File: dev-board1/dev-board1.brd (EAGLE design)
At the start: 100 x 80 mm, 127 parts, among them IC1 MSP432E401, IC2 MT48LC16M16A2, IC3 SIM800C, IC4 CC3100MOD-LWK, IC5 TPD3E001DRL, IC6 TPD3E001DRL, IC7 TPD3E001DRL, IC8 BQ25601, IC9 TPS62082, J1 MAGJACK-RJMG16XXX-8, J2 SIM-78723-1001, J3 ER-TFT024-3, J4 SWD_SHROUD, Q6 CSD25402Q3A, U3 ER-TFT024-3-OUTLINE, X2 BU-SMA-V

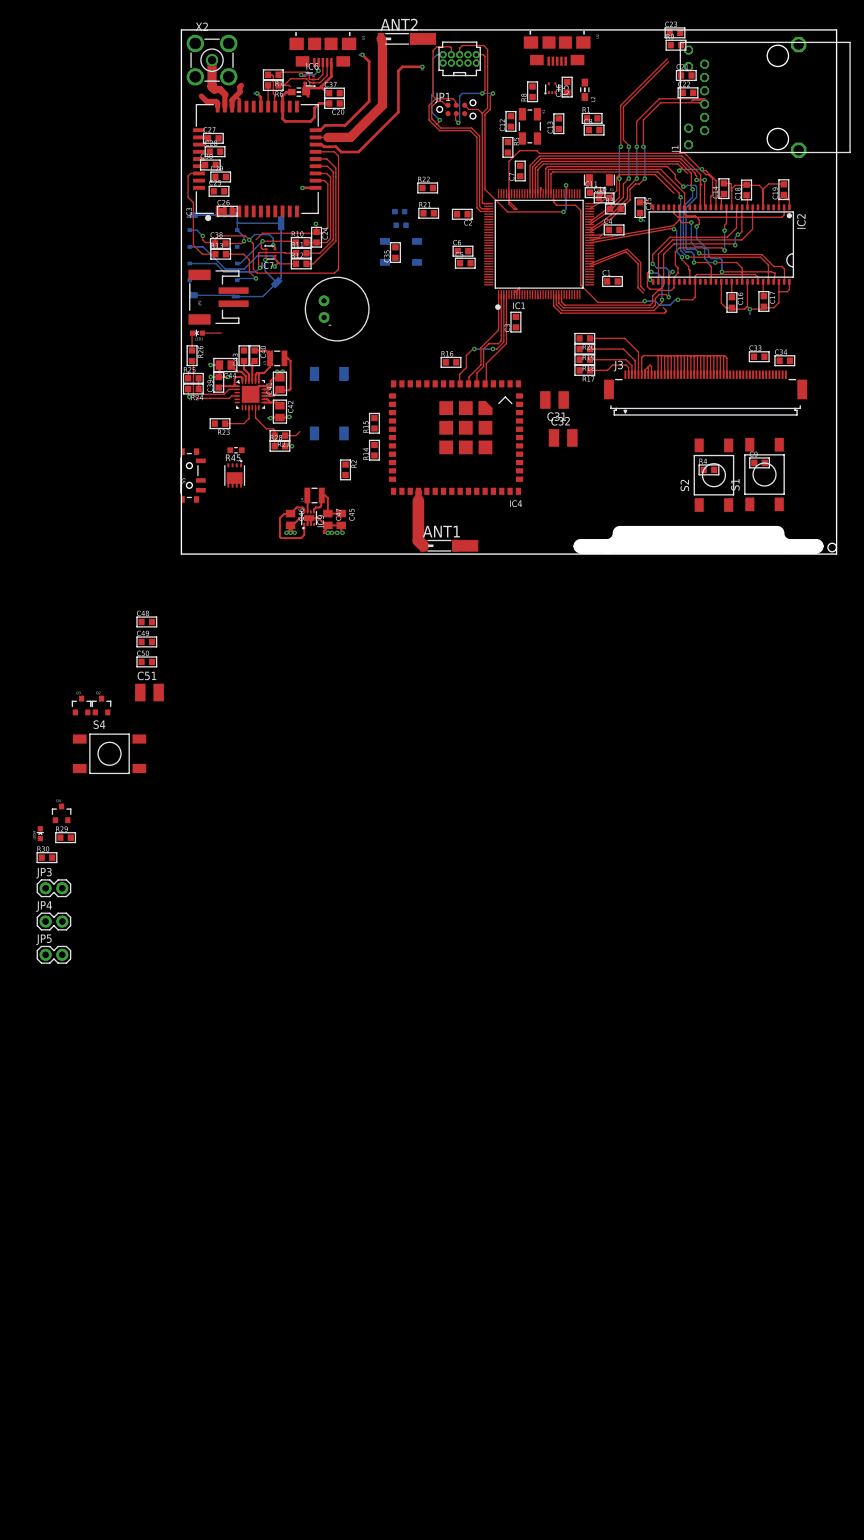
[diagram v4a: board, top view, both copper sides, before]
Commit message: changing to cc3120miod
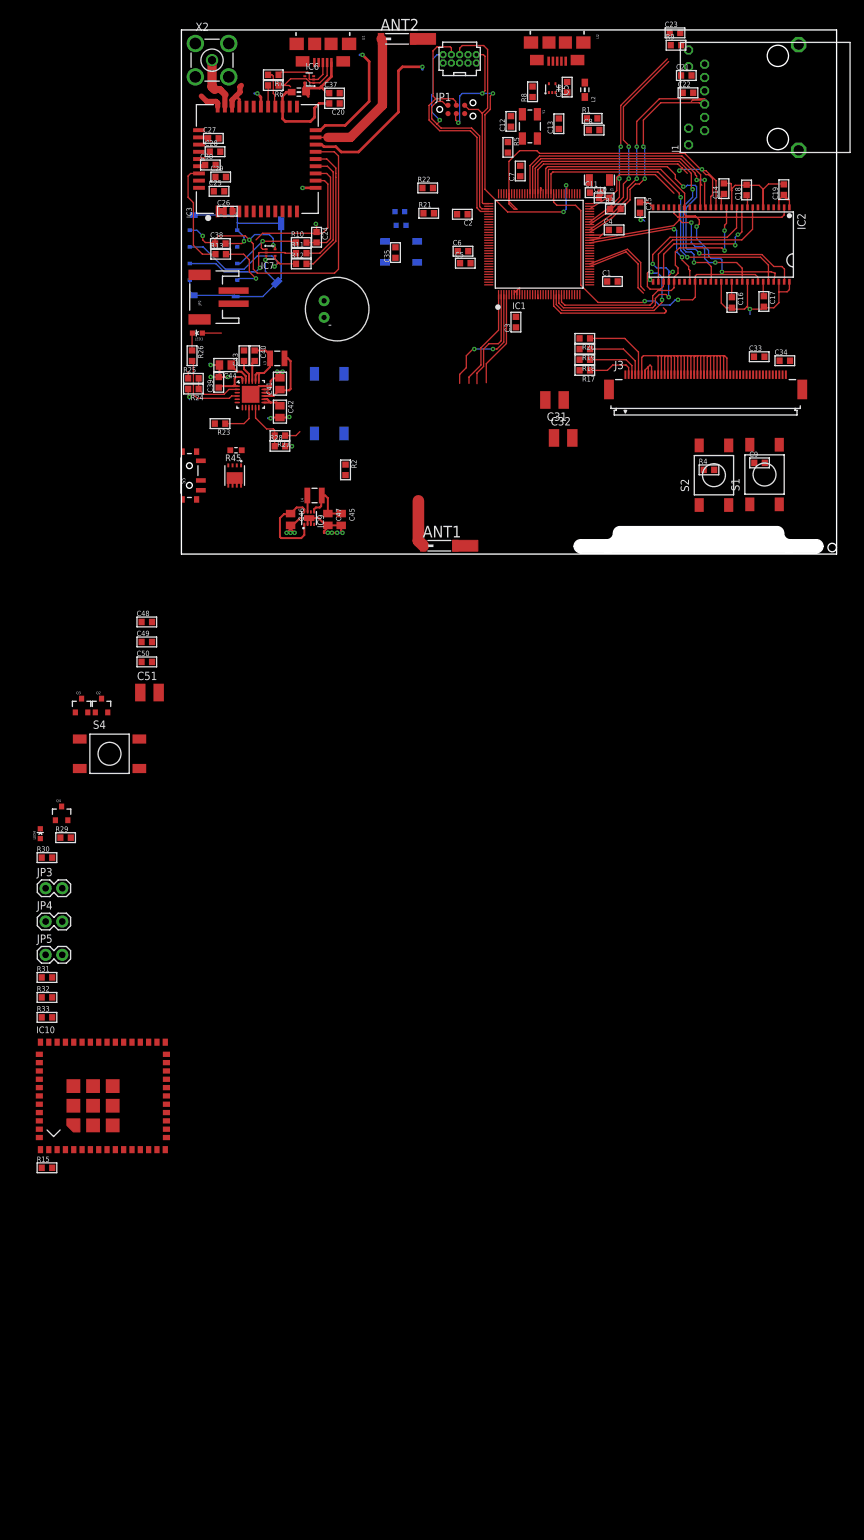
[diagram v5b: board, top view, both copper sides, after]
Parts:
- removed IC4: CC3100MOD-LWK, TiLDA Mk4 Parts:CC3100MOD-LWK
- removed R14: 10k, passives-7351:R0603-N
- removed R16: 220k, passives-7351:R0603-N
- added IC10: CC3120MOD, TiLDA Mk4 Parts:CC3100MOD-LWK
- added R31, R32, R33: dnp, passives-7351:R0603-N
- R15: value 220k -> 100k
- moved R15 124.1 mm to (-20.5, -93.7), turned to 0 degrees
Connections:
- removed net N$36: IC4.23, R14.1
- removed net N$37: IC4.21, R15.1
- removed net N$38: IC4.10, R16.1
- removed net N$42: IC6.4, U1.ID
- removed net VABT_SWTICHED: Q6.1, Q6.2, Q6.3
- removed net VBAT: Q6.5, Q6.6, Q6.7, Q6.8, Q6.EP, R45.1
- new net N$50: C31.1, C32.1, IC10.36, IC10.37, IC10.40, JP3.2, R32.1
- new net VBAT_SWITCHED: C46.1, IC9.1, IC9.8, JP4.1, Q6.1, Q6.2, Q6.3, R31.2
- new net VBAT_UNSWITCH: JP5.2, Q6.5, Q6.6, Q6.7, Q6.8, Q6.EP, R33.1, R45.1
- net +3V3: now also R32.2; no longer C31.1, C32.1, IC4.36, IC4.37, IC4.40, JP3.2
- net CC_CLK: now also IC10.5; no longer IC4.5
- net CC_CS: now also IC10.8; no longer IC4.8
- net CC_MISO: now also IC10.7; no longer IC4.7
- net CC_MOSI: now also IC10.6; no longer IC4.6
- net CC_RX: now also IC10.47; no longer IC4.47
- net CC_TX: now also IC10.46; no longer IC4.46
- net GND: now also IC10.1, IC10.16, IC10.2, IC10.27, IC10.28, IC10.30, IC10.32, IC10.38, IC10.43, IC10.55, IC10.56, IC10.57, IC10.58, IC10.59, IC10.60, IC10.61, IC10.62, IC10.63; no longer IC4.1, IC4.16, IC4.2, IC4.27, IC4.28, IC4.30, IC4.32, IC4.38, IC4.43, IC4.55, IC4.56, IC4.57, IC4.58, IC4.59, IC4.60, IC4.61, IC4.62, IC4.63, R14.2, R16.2
- net N$39: now also IC10.35; no longer IC4.35
- net N$45: now also JP4.2, R31.1
- net N$48: now also IC10.31; no longer IC4.31
- net N$49: now also IC10.4, R15.1; no longer IC4.4
- net N$54: now also IC10.11; no longer IC4.11
- net V_UNREG: now also R33.2; no longer C46.1, IC9.1, IC9.8, JP4.1
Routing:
- net VBAT_SWITCHED: track 0.00 -> 13.4 mm
- net V_UNREG: track 25.8 -> 12.4 mm
- net N$42: track 4.79 -> 0.00 mm, vias 2 -> 0
- net N$48: track 8.63 -> 7.20 mm

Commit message: all major connections done
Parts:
- added C52, C53, C54: 10p, passives-7351:C0603-N
- added C55, C56, C57: 33p, passives-7351:C0603-N
- added LED5: red, TiLDA Mk4 Parts:LED-0603
- added R14, R16: 470, passives-7351:R0603-N
- added R34: 2k, passives-7351:R0603-N
- added S6: (no value), Switches:6MMTACTSM
- moved IC10 114.1 mm to (41.9, 17.9), turned to 180 degrees
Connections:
- removed net N$43: IC3.10
- removed net N$44: IC3.9
- removed net N$49: IC10.4, R15.1
- removed net N$52: Q2.1
- removed net N$54: IC10.11
- removed net N$55: IC3.42
- removed net N$61: J3.10
- removed net N$65: Q3.1
- removed net N$69: R22.2
- removed net N$70: R21.2
- removed net N$71: D1.4
- removed net N$72: IC1.18
- removed net N$80: IC8.5
- removed net N$81: IC8.6
- removed net N$82: IC8.7
- removed net VCC: JP1.1
- new net BQ_INT: IC1.124, IC8.7
- new net BQ_SCL: IC1.121, IC8.5
- new net BQ_SDA: IC1.120, IC8.6
- new net CC_HIB: IC1.14, IC10.4, R15.1
- new net CC_IRQ: IC1.15, IC10.11
- new net CC_RST: IC1.18, IC10.35, S6.3, S6.4
- new net ETHLED0: IC1.63, R14.1
- new net ETHLED1: IC1.61, R16.1
- new net ETHLED2: IC1.43, R34.2
- new net LCD_BLIGHT: IC1.42, Q2.1
- new net LCD_DCX: IC1.20, J3.36
- new net LCD_RST: IC1.21, J3.10
- new net LCD_TEAR: IC1.19, J3.39
- new net LEDA: IC1.95, R21.2
- new net LEDB: IC1.96, R22.2
- new net N$36: IC1.44
- new net N$37: IC1.45
- new net N$38: C52.1, C53.2, C55.1, C56.2, IC3.9, U$1.1
- new net N$42: C53.1, C54.2, C56.1, C57.2, IC3.10, U$1.2
- new net NETLIGHT: IC1.105, IC3.41, Q4.1, R29.2
- new net NPIX: D1.4, IC1.123
- new net PWR_KEY: IC1.102, Q3.1
- new net SIM_STATUS: IC1.106, IC3.42
- net +3V3: now also J3.35, JP1.1
- net GND: now also C52.2, C54.1, C55.2, C57.1, J1.7, J1.9, LED5.C, S6.1, S6.2
- net N$25: now also J1.8, R14.2; no longer IC3.41, Q4.1, R29.2
- net N$26: now also J1.10, R16.2; no longer J3.36
- net N$39: now also LED5.A, R34.1; no longer IC10.35
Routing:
- net +3V3: track 38.2 -> 54.3 mm
- net GND: track 282.6 -> 298.7 mm, vias 26 -> 28

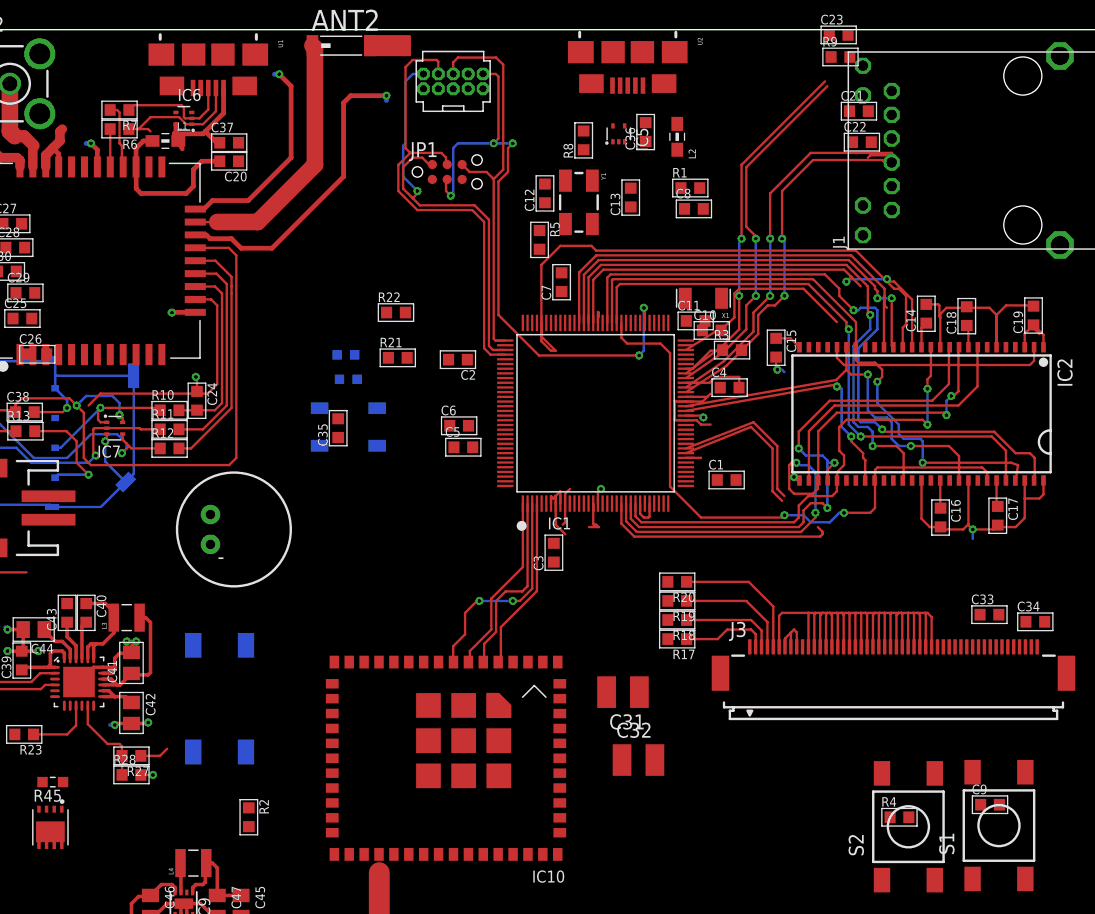
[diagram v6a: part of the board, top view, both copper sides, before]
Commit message: testpoints added
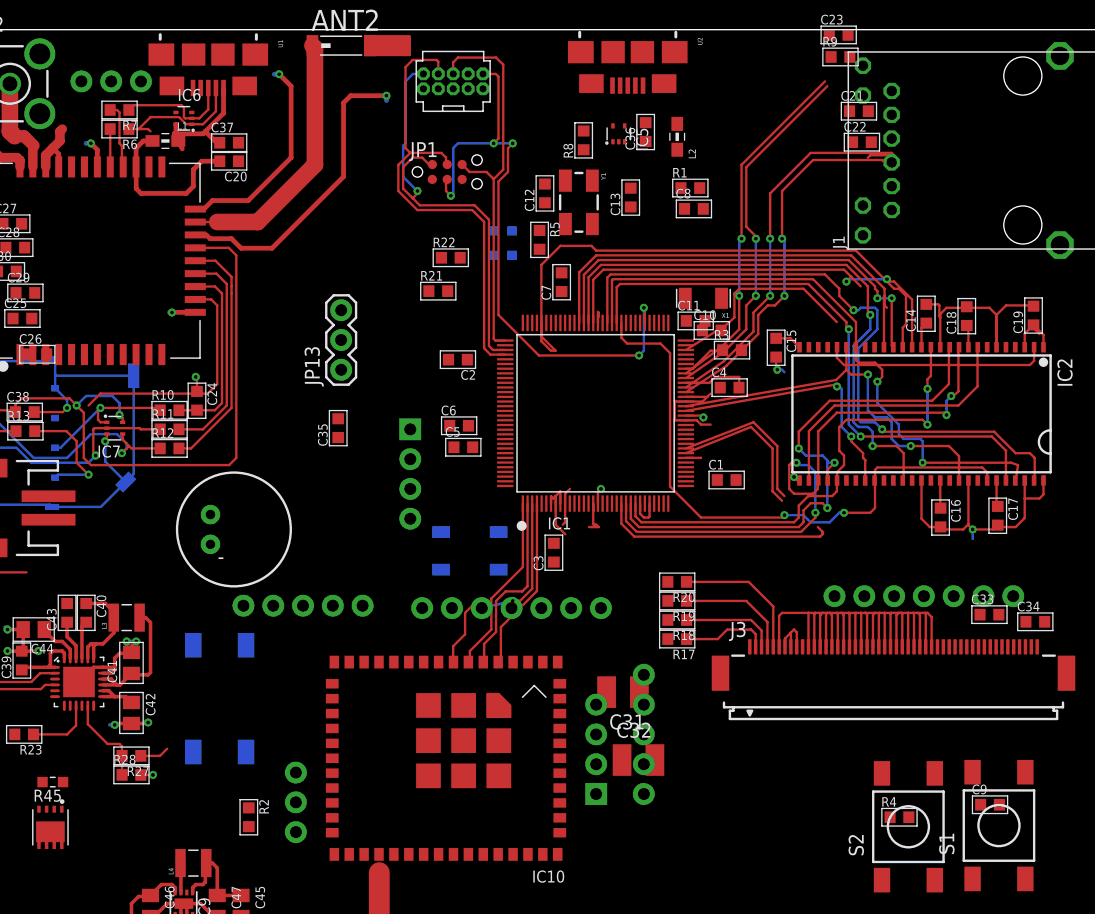
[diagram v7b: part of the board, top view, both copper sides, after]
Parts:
- added JP10, JP8: (no value), TiLDA Mk4 Parts:1X04
- added JP11, JP13, JP14: (no value), TiLDA Mk4 Parts:1X03
- added JP12, JP9: (no value), TiLDA Mk4 Parts:1X05
- added JP6, JP7: (no value), TiLDA Mk4 Parts:1X07
- moved LED2 17.1 mm to (46.7, 62.8)
- moved LED1 16.9 mm to (46.7, 60.8)
- moved D1 14.8 mm to (43.9, 35.6)
- moved R21 6.66 mm to (41.2, 57.7)
- moved R22 6.61 mm to (42.3, 60.6)
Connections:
- new net N$43: IC10.48, JP10.1
- new net N$44: IC10.44, JP9.3
- new net N$49: IC10.51, JP9.2
- new net N$51: IC10.49, JP10.2
- new net N$52: IC10.50, JP10.3
- new net N$54: IC10.52, JP10.4
- new net N$55: IC10.34, JP11.1
- new net N$61: IC10.24, JP11.2
- new net N$65: IC10.23, JP11.3
- new net N$66: IC10.14, JP12.2
- new net N$69: IC10.15, JP12.3
- new net N$70: IC10.17, JP12.4
- new net N$71: IC10.13, JP12.5
- new net N$72: IC3.23, JP14.2
- new net N$77: IC3.22, JP14.3
- net BQ_INT: now also JP8.2
- net BQ_SCL: now also JP8.4
- net BQ_SDA: now also JP8.3
- net CC_CLK: now also JP7.6
- net CC_CS: now also JP7.3
- net CC_HIB: now also JP7.7
- net CC_IRQ: now also JP7.2
- net CC_MISO: now also JP7.4
- net CC_MOSI: now also JP7.5
- net CC_RX: now also JP9.4
- net CC_TX: now also JP9.5
- net GND: now also JP12.1, JP13.1, JP14.1, JP6.1, JP7.1, JP8.1, JP9.1
- net LCD_CLK: now also JP6.7
- net LCD_CS: now also JP6.6
- net LCD_DCX: now also JP6.2
- net LCD_MISO: now also JP6.4
- net LCD_MOSI: now also JP6.5
- net LCD_TEAR: now also JP6.3
- net SIM_RX: now also JP13.2
- net SIM_TX: now also JP13.3

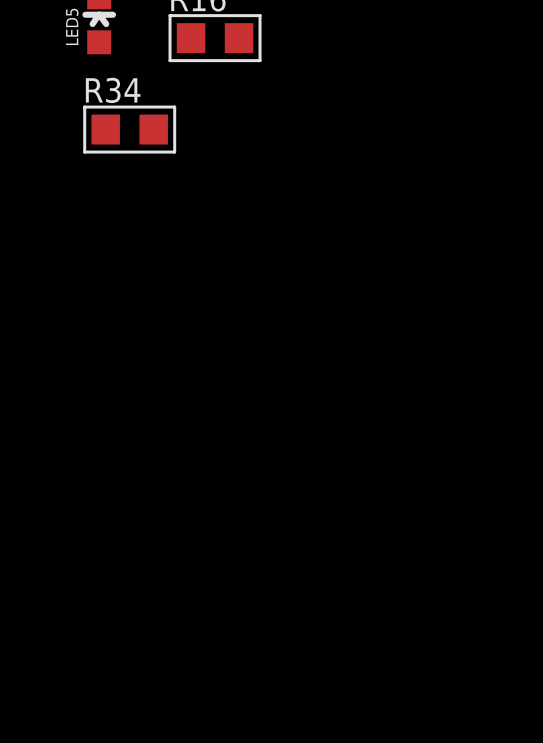
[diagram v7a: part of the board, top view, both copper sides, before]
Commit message: a few single testpoints
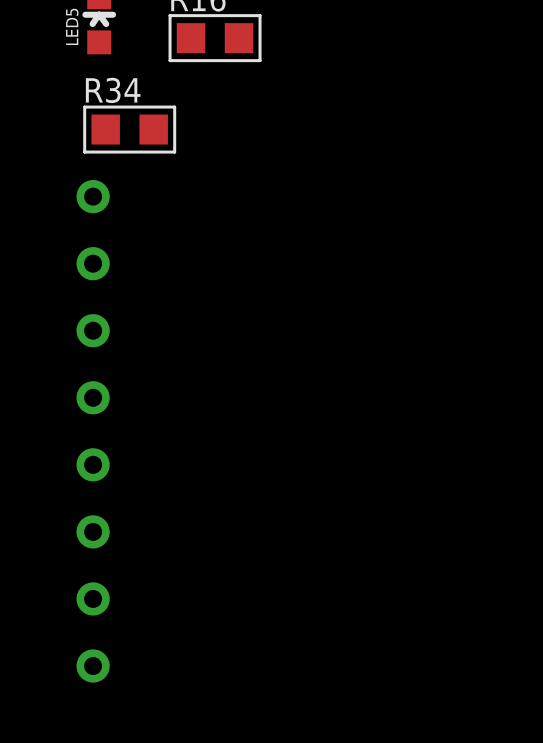
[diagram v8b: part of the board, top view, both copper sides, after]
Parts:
- added TP1, TP2, TP3, TP4, TP5, TP6, TP7, TP8: TP, Testpoint:TP
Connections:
- new net N$80: IC1.65, TP7.P$1
- net +3V3: now also TP8.P$1
- net CC_RST: now also TP2.P$1
- net N$40: now also TP5.P$1
- net N$41: now also TP6.P$1
- net N$79: now also TP1.P$1
- net NETLIGHT: now also TP4.P$1
- net SIM_STATUS: now also TP3.P$1
